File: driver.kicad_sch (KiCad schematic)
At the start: 8 parts, among them U5 74AHC04, U6 74LS08, U8 74LS08, U9 74LS08

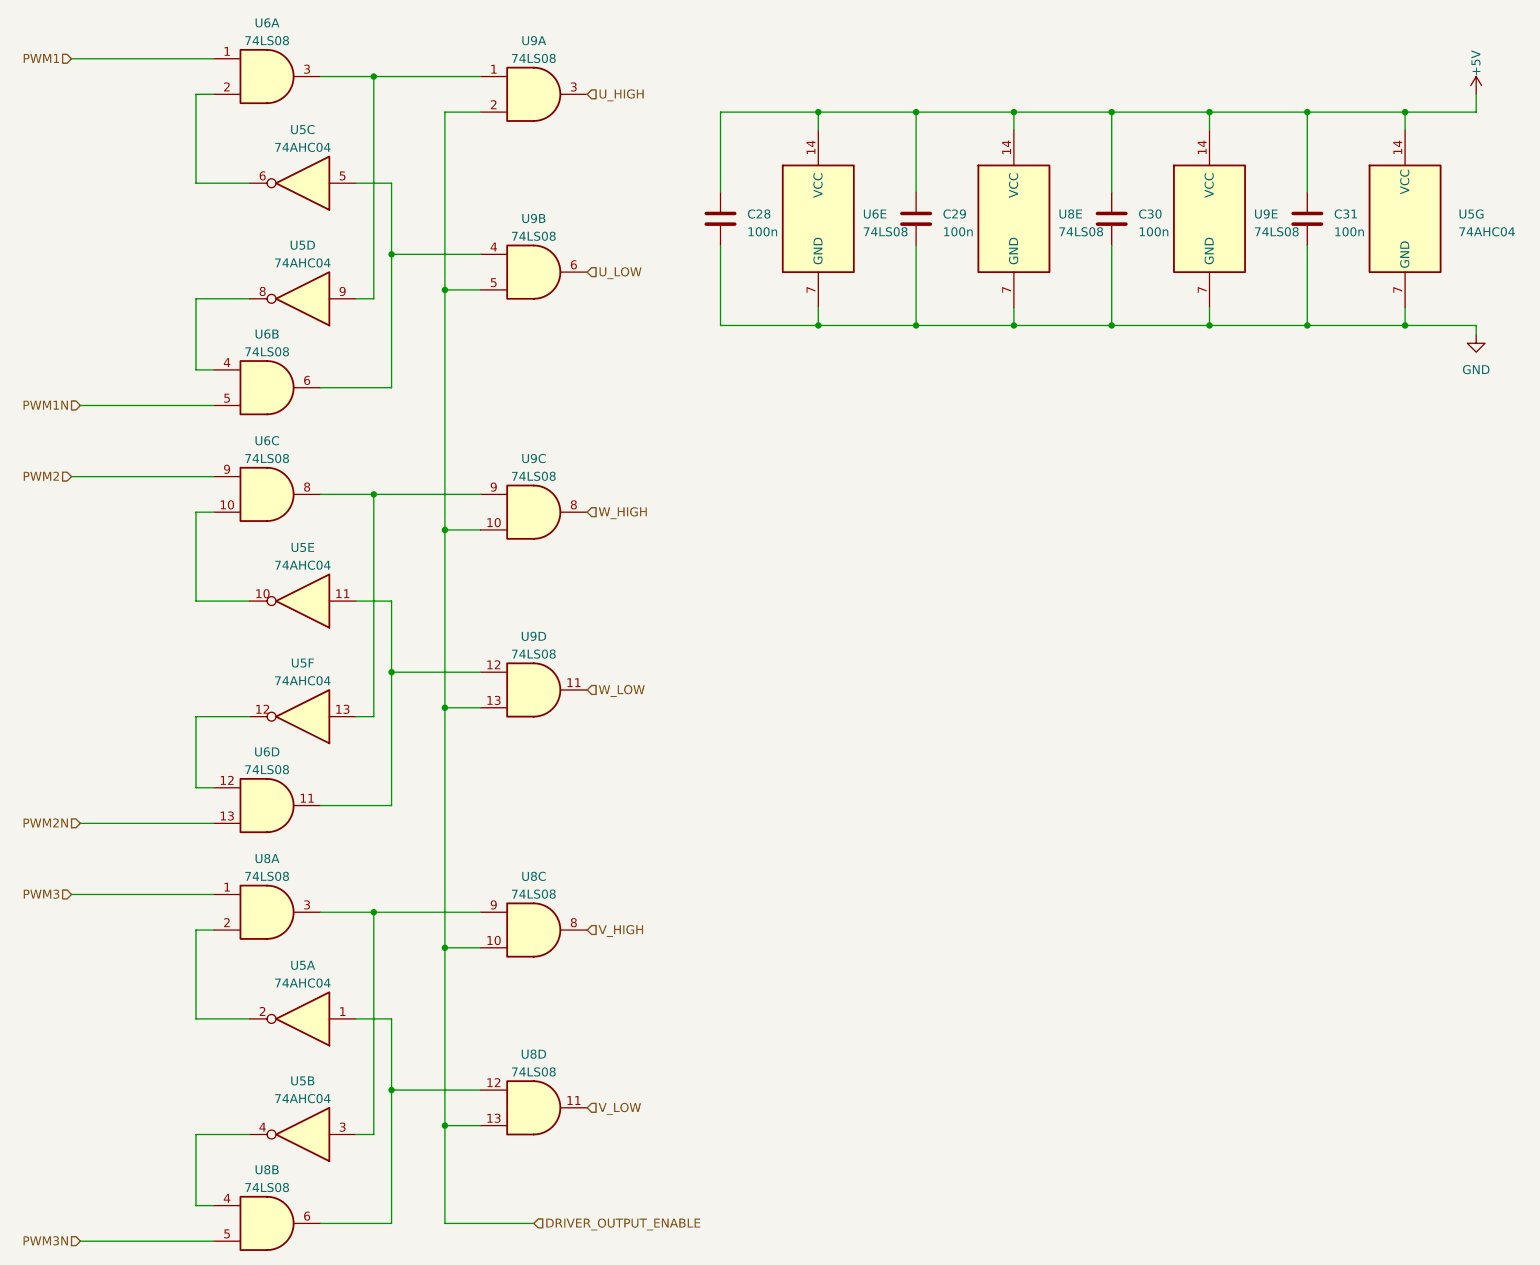
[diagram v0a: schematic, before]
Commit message: Added current sensing
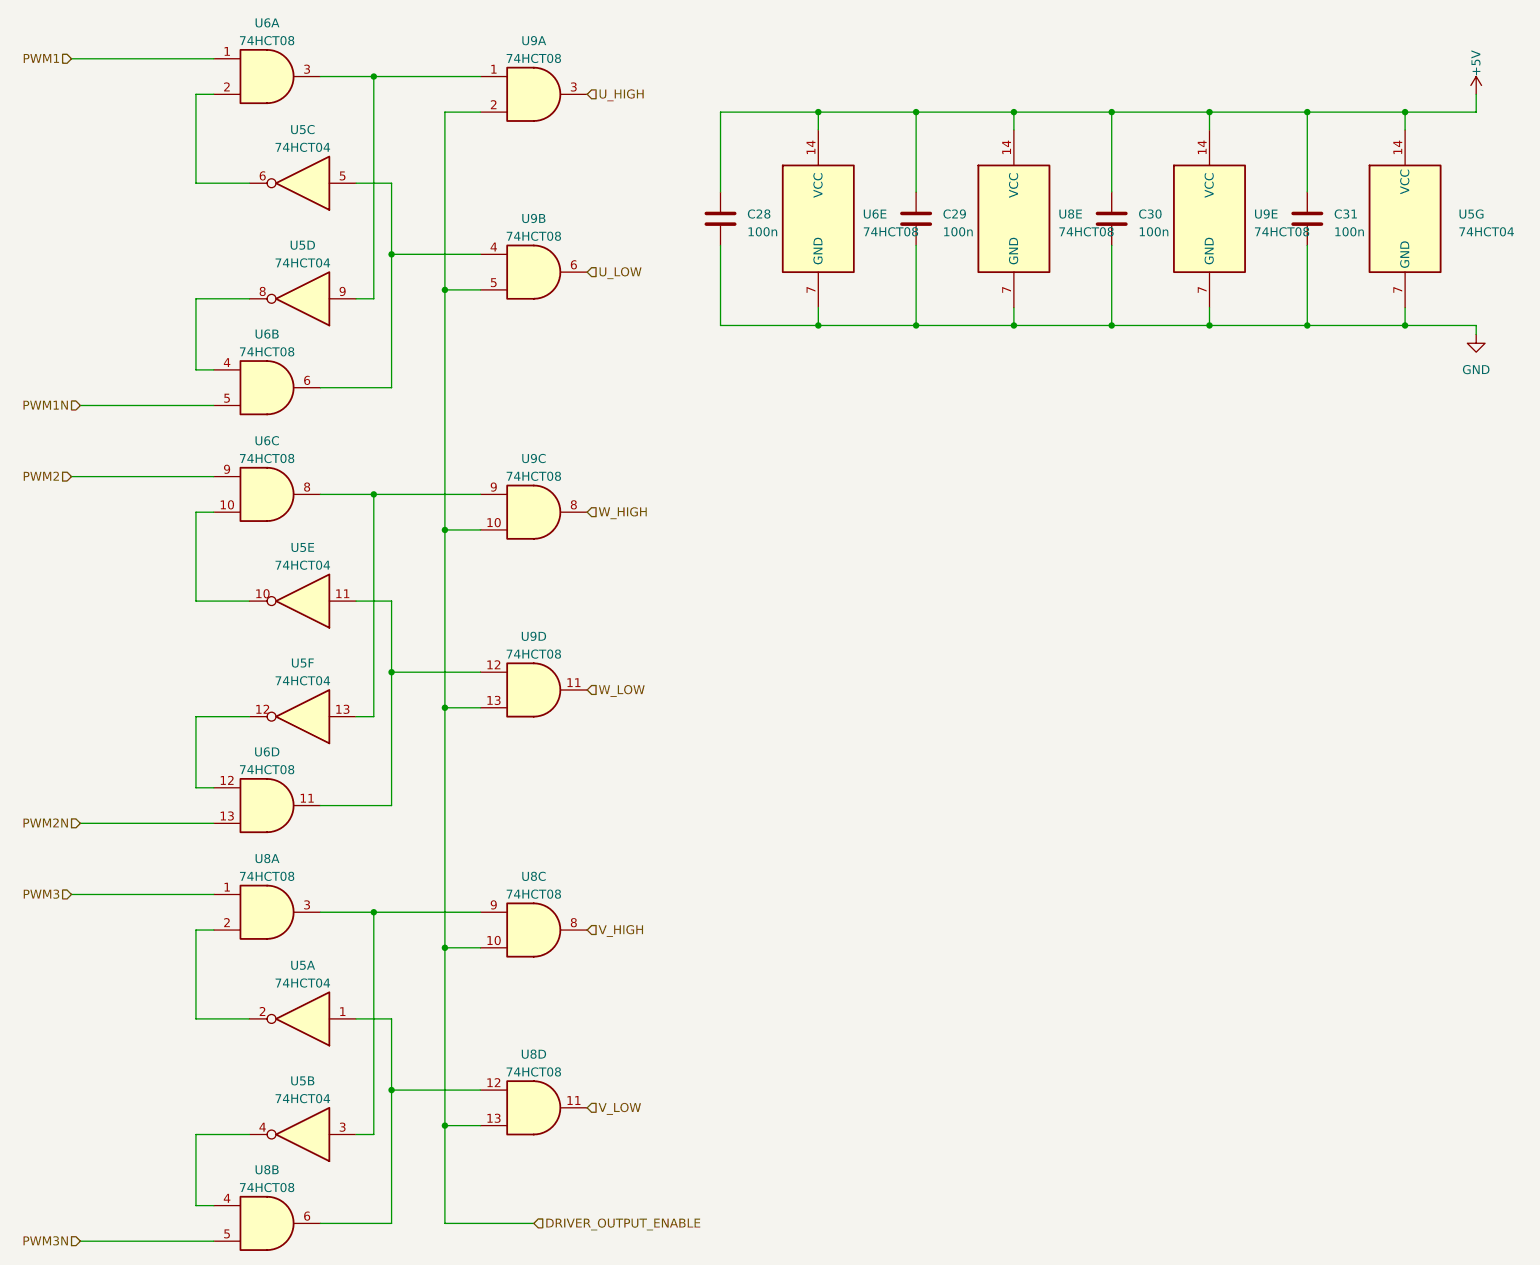
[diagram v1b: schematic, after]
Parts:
- U5: value 74AHC04 -> 74HCT04
- U6, U8, U9: value 74LS08 -> 74HCT08
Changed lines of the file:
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@@
       (effects (font (size 1.27 1.27)))
     )
-    (property "Value" "74LS08" (at 63.4917 182.88 0)
+    (property "Value" "74HCT08" (at 63.4917 182.88 0)
       (effects (font (size 1.27 1.27)))
     )
@@
       (effects (font (size 1.27 1.27)))
     )
-    (property "Value" "74LS08" (at 101.5917 21.59 0)
+    (property "Value" "74HCT08" (at 101.5917 21.59 0)
       (effects (font (size 1.27 1.27)))
     )
@@
       (effects (font (size 1.27 1.27)))
     )
-    (property "Value" "74LS08" (at 101.5917 81.28 0)
+    (property "Value" "74HCT08" (at 101.5917 81.28 0)
       (effects (font (size 1.27 1.27)))
     )
@@
       (effects (font (size 1.27 1.27)) (justify left))
     )
-    (property "Value" "74LS08" (at 148.59 46.355 0)
+    (property "Value" "74HCT08" (at 148.59 46.355 0)
       (effects (font (size 1.27 1.27)) (justify left))
     )
@@
       (effects (font (size 1.27 1.27)) (justify left))
     )
-    (property "Value" "74LS08" (at 204.47 46.355 0)
+    (property "Value" "74HCT08" (at 204.47 46.355 0)
       (effects (font (size 1.27 1.27)) (justify left))
     )
@@
       (effects (font (size 1.27 1.27)))
     )
-    (property "Value" "74LS08" (at 63.4917 138.43 0)
+    (property "Value" "74HCT08" (at 63.4917 138.43 0)
       (effects (font (size 1.27 1.27)))
     )
@@
       (effects (font (size 1.27 1.27)) (justify left))
     )
-    (property "Value" "74LS08" (at 176.53 46.355 0)
+    (property "Value" "74HCT08" (at 176.53 46.355 0)
       (effects (font (size 1.27 1.27)) (justify left))
     )
@@
       (effects (font (size 1.27 1.27)))
     )
-    (property "Value" "74LS08" (at 63.4917 63.5 0)
+    (property "Value" "74HCT08" (at 63.4917 63.5 0)
       (effects (font (size 1.27 1.27)))
     )
@@
       (effects (font (size 1.27 1.27)))
     )
-    (property "Value" "74AHC04" (at 68.58 50.8 0)
+    (property "Value" "74HCT04" (at 68.58 50.8 0)
       (effects (font (size 1.27 1.27)))
     )
@@
       (effects (font (size 1.27 1.27)))
     )
-    (property "Value" "74LS08" (at 101.5917 106.68 0)
+    (property "Value" "74HCT08" (at 101.5917 106.68 0)
       (effects (font (size 1.27 1.27)))
     )
@@
       (effects (font (size 1.27 1.27)) (justify left))
     )
-    (property "Value" "74AHC04" (at 233.68 46.355 0)
+    (property "Value" "74HCT04" (at 233.68 46.355 0)
       (effects (font (size 1.27 1.27)) (justify left))
     )
@@
       (effects (font (size 1.27 1.27)))
     )
-    (property "Value" "74AHC04" (at 68.58 170.18 0)
+    (property "Value" "74HCT04" (at 68.58 170.18 0)
       (effects (font (size 1.27 1.27)))
     )
@@
       (effects (font (size 1.27 1.27)))
     )
-    (property "Value" "74LS08" (at 101.5917 166.37 0)
+    (property "Value" "74HCT08" (at 101.5917 166.37 0)
       (effects (font (size 1.27 1.27)))
     )
@@
       (effects (font (size 1.27 1.27)))
     )
-    (property "Value" "74LS08" (at 63.4917 19.05 0)
+    (property "Value" "74HCT08" (at 63.4917 19.05 0)
       (effects (font (size 1.27 1.27)))
     )
@@
       (effects (font (size 1.27 1.27)))
     )
-    (property "Value" "74AHC04" (at 68.58 34.29 0)
+    (property "Value" "74HCT04" (at 68.58 34.29 0)
       (effects (font (size 1.27 1.27)))
     )
@@
       (effects (font (size 1.27 1.27)))
     )
-    (property "Value" "74LS08" (at 63.4917 78.74 0)
+    (property "Value" "74HCT08" (at 63.4917 78.74 0)
       (effects (font (size 1.27 1.27)))
     )
@@
       (effects (font (size 1.27 1.27)))
     )
-    (property "Value" "74LS08" (at 63.4917 123.19 0)
+    (property "Value" "74HCT08" (at 63.4917 123.19 0)
       (effects (font (size 1.27 1.27)))
     )
@@
       (effects (font (size 1.27 1.27)))
     )
-    (property "Value" "74LS08" (at 101.5917 140.97 0)
+    (property "Value" "74HCT08" (at 101.5917 140.97 0)
       (effects (font (size 1.27 1.27)))
     )
@@
       (effects (font (size 1.27 1.27)))
     )
-    (property "Value" "74AHC04" (at 68.58 93.98 0)
+    (property "Value" "74HCT04" (at 68.58 93.98 0)
       (effects (font (size 1.27 1.27)))
     )
@@
       (effects (font (size 1.27 1.27)))
     )
-    (property "Value" "74AHC04" (at 68.58 153.67 0)
+    (property "Value" "74HCT04" (at 68.58 153.67 0)
       (effects (font (size 1.27 1.27)))
     )
@@
       (effects (font (size 1.27 1.27)))
     )
-    (property "Value" "74AHC04" (at 68.58 110.49 0)
+    (property "Value" "74HCT04" (at 68.58 110.49 0)
       (effects (font (size 1.27 1.27)))
     )
@@
       (effects (font (size 1.27 1.27)))
     )
-    (property "Value" "74LS08" (at 101.5917 46.99 0)
-      (effects (font (size 1.27 1.27)))
-    )
+    (property "Value" "74HCT08" (at 101.5917 46.99 0)
+      (effects (font (size 1.27 1.27)))
+    )

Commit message: Preliminary footprints
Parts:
- removed C28, C29, C30, C31: 100n, symbol Device:C
- added C1 (x4): 1u, Capacitor_SMD:C_0402_1005Metric_Pad0.74x0.62mm_HandSolder, symbol Device:C
- U5: footprint (none) -> Package_SO:SOIC-14_3.9x8.7mm_P1.27mm; LCSC (none) -> C553166
- U6, U8, U9: footprint (none) -> Package_SO:SOIC-14_3.9x8.7mm_P1.27mm; LCSC (none) -> C900098
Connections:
- net +5V: now also C1.1, C1.1, C1.1, C1.1
- net GND: now also C1.2, C1.2, C1.2, C1.2
